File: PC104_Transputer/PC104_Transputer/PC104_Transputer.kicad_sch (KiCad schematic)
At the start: 32 parts, among them J3 Conn_02x08_Odd_Even, J5 Conn_02x05_Odd_Even, U11 IMSC011, U2 74LS244_Split, U4 74HC245, U8 TRAM, Y1 CXO_DIP8

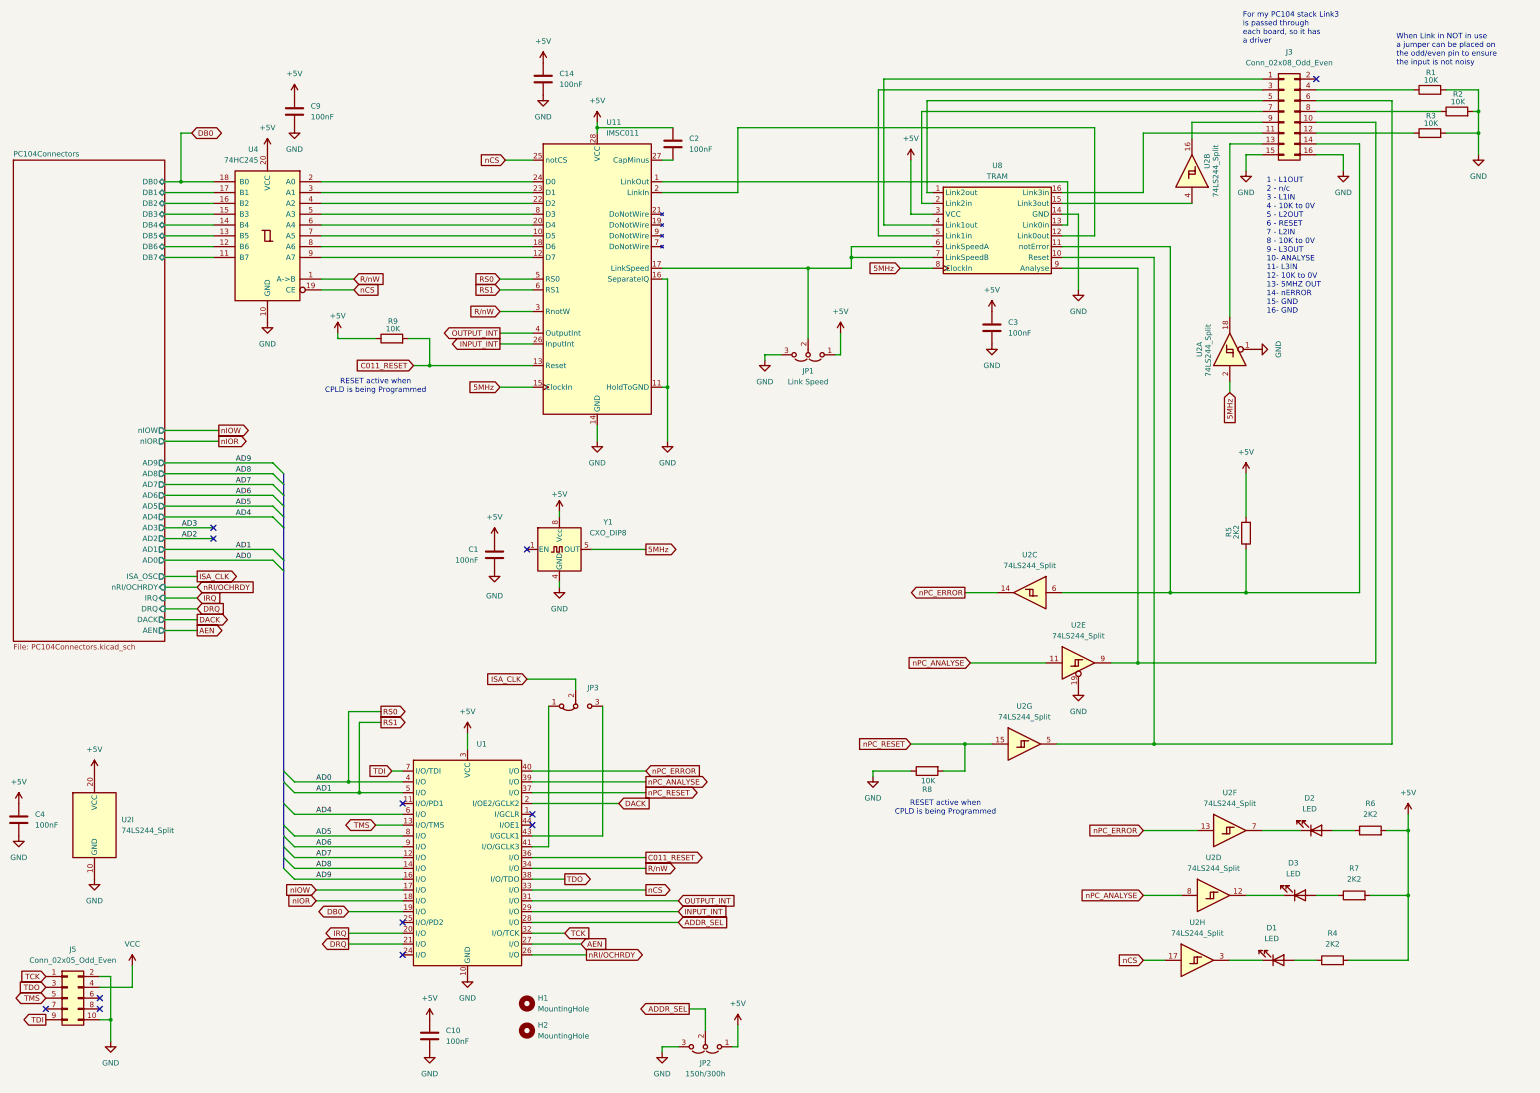
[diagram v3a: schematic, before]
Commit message: Added extra jumpers to transputer board
I also moved the downstream link to the same place as the upstream on the dual TRAM card.
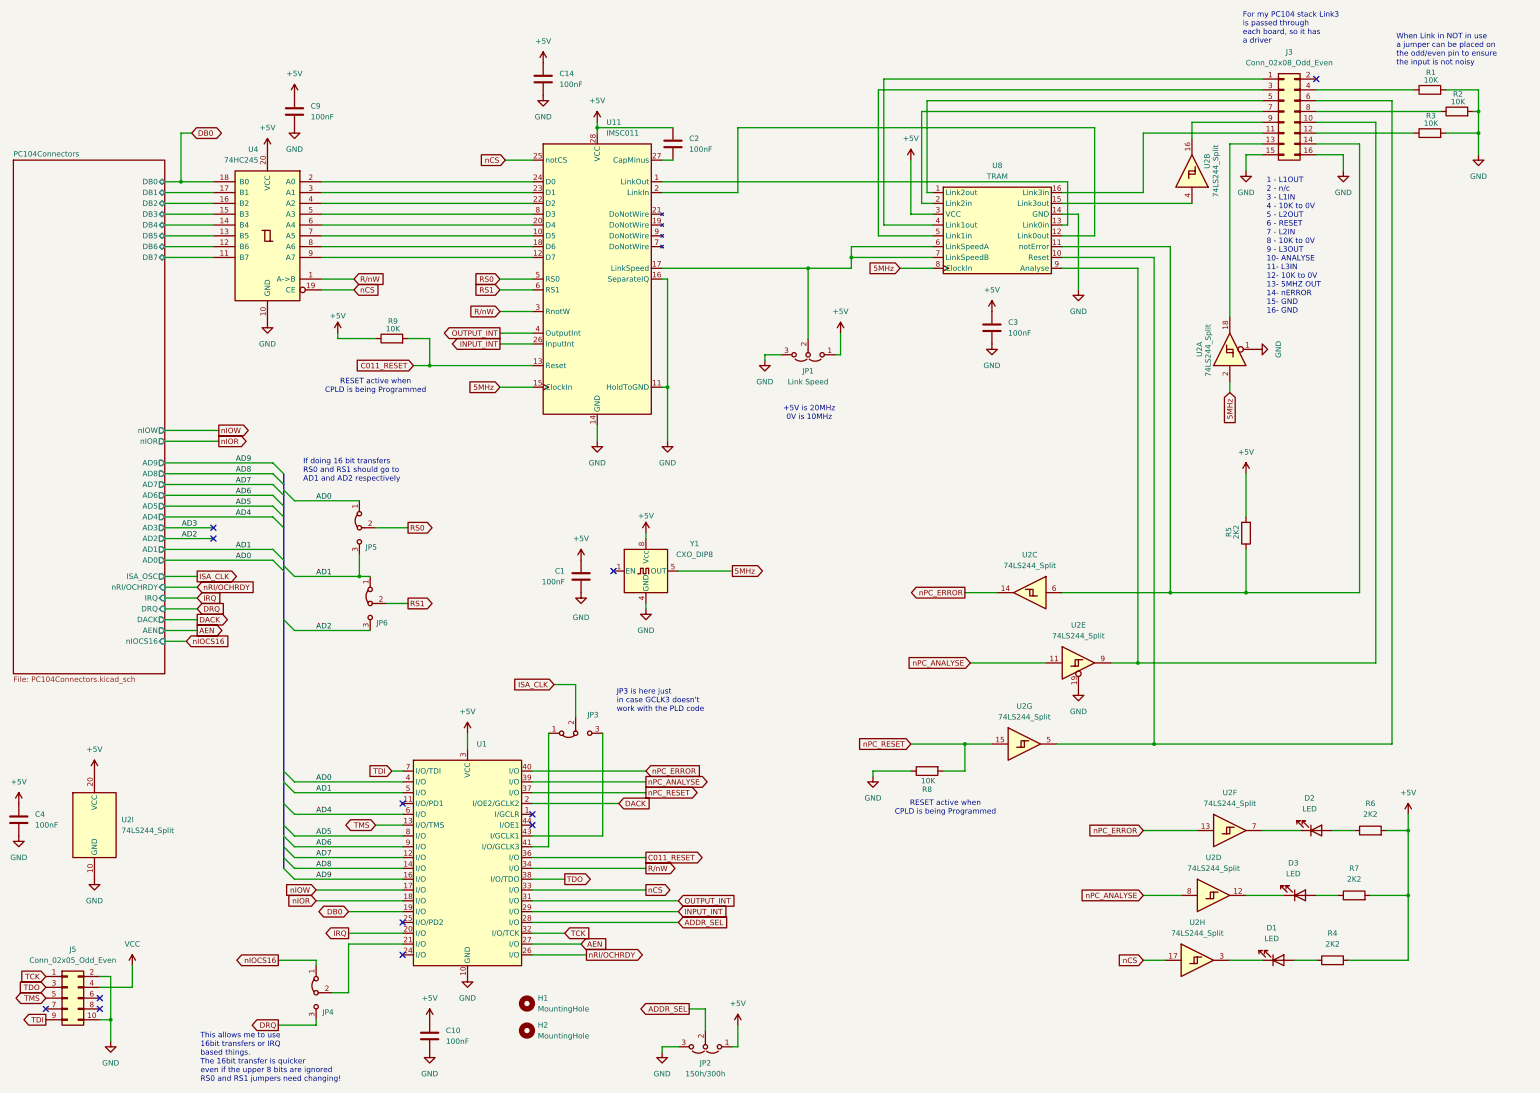
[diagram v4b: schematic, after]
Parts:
- added JP4, JP5, JP6: Jumper_3_Bridged12, Jumper:SolderJumper-3_P1.3mm_Bridged12_RoundedPad1.0x1.5mm_NumberLabels, symbol Jumper:Jumper_3_Bridged12
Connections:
- net AD2: now also JP6.3 (B)
- net DRQ: now also JP4.3 (B); no longer U1.21 (I/O)
- net RS0: now also JP5.2 (C); no longer U1.4 (I/O)
- net RS1: now also JP6.2 (C); no longer U1.5 (I/O)
- new net: JP4.2 (C), U1.21 (I/O)
- new net AD0: JP5.1 (A), U1.4 (I/O)
- new net AD1: JP5.3 (B), JP6.1 (A), U1.5 (I/O)
- new net nIOCS16: JP4.1 (A)
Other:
- sheet PC104Connectors ports: added nIOCS16; removed none
- note added: "+5V is 20MHz 0V is 10MHz"
- note added: "If doing 16 bit transfers RS0 and RS1 should go to AD1 and AD2 respectively"
- note added: "JP3 is here just in case GCLK3 doesn't work with the PLD code"
- note added: "This allows me to use 16bit transfers or IRQ based things. The 16bit transfer is quicker even if the upper 8 bits are ignored RS0 and RS1 jumpers need changing!"
- moved on the sheet: C1, JP3, Y1

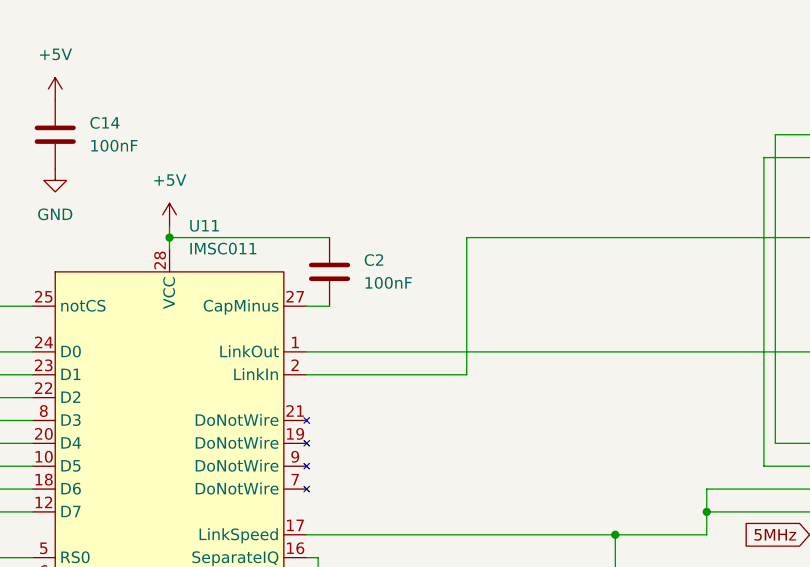
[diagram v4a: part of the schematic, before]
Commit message: Board assembled, work on CPLD code
I found a bunch of mistakes in the CPLD equations, it's still not quite right yet
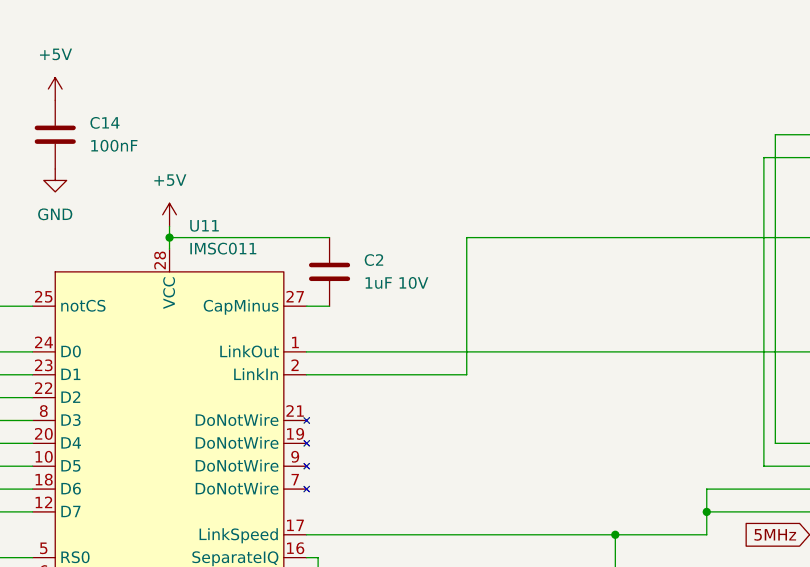
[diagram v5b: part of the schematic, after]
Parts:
- C2: value 100nF -> 1uF 10V
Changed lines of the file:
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@@
 			)
 		)
-		(property "Value" "100nF"
+		(property "Value" "1uF 10V"
 			(at 209.55 53.3399 0)
 			(effects
